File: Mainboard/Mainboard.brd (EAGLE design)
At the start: 90 x 150 mm, 9 parts, among them J1 USB3076-XX-X_REVC, J2 640455-5, J3 640455-2, J4 640455-4, J5 640455-4, J6 SJ-3523-SMT-TR, J7 640455-2, J8 929850-01-06-RB

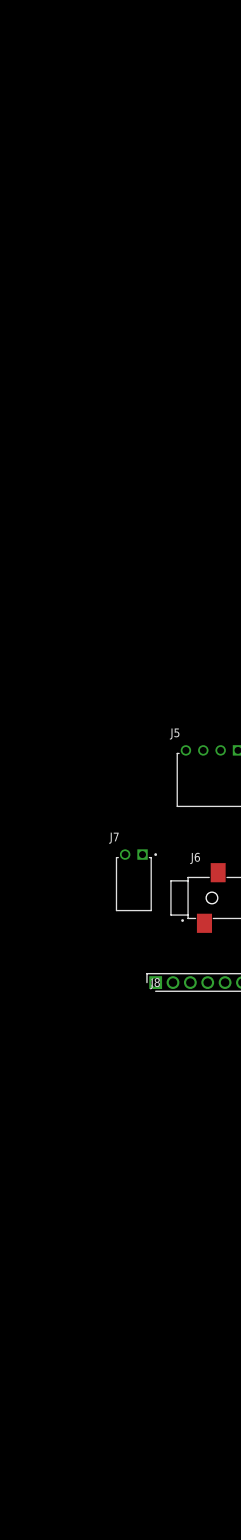
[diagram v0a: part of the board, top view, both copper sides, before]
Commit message: Mainboard updated
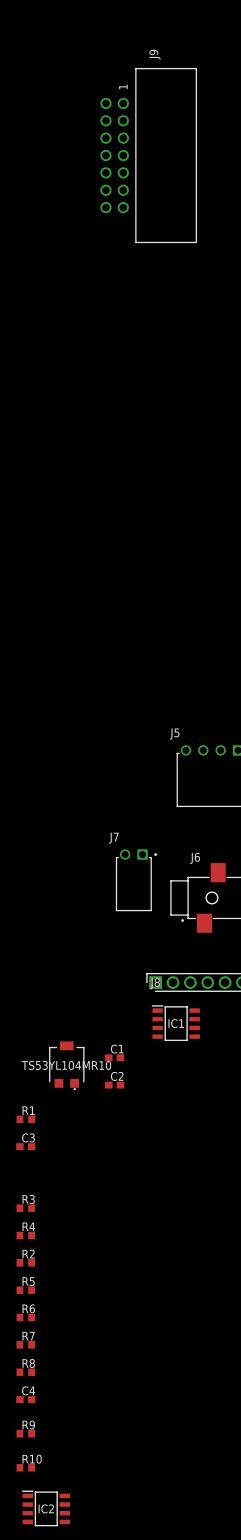
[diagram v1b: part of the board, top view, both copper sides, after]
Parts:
- added C1, C2: 100n, rcl:C0603
- added C3, C4: 1u, rcl:C0603
- added IC1: TL072CD, SamacSys_Parts:SOIC127P600X175-8N
- added IC2: LM386M-1_NOPB, SamacSys_Parts:SOIC127P600X175-8N
- added J9: 61201421721, 61201421721:61201421721
- added R1, R9: 10k, rcl:R0603
- added R10, R2, R3: 0, rcl:R0603
- added R4: NP_0, rcl:R0603
- added R5: 4k7, rcl:R0603
- added R6: 15k, rcl:R0603
- added R7: 33k, rcl:R0603
- added R8: 100, rcl:R0603
- added TS53YL104MR10: 100k, SamacSys_Parts:TS53YL203MR10
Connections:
- net E5V_CN11 renamed N$1
- removed net GND_CN12: A1.CN12_20, A1.CN12_39, A1.CN12_54, A1.CN12_63, A1.CN12_71, A1.CN12_72, A1.CN12_9
- new net +3V3: J9.8
- new net 1_IN+: C3.2, IC1.3, R1.2, R5.1
- new net 1_IN-: IC1.2, R2.1
- new net 1_OUT: C3.1, IC1.1, R3.1
- new net 2_IN-: IC1.6, R6.2, R7.1
- new net 2_OUT: IC1.7, R7.2, R8.1
- new net ADC_POTI: J9.9
- new net BUTTON_BACK: J9.13
- new net BUTTON_ENTER: J9.14
- new net DAC_OUT1: R10.1
- new net DISP_BUSY: J9.1
- new net DISP_CLK: J9.5
- new net DISP_CS: J9.4
- new net DISP_DC: J9.3
- new net DISP_DIN: J9.6
- new net DISP_RST: J9.2
- new net JOYSTICK_SW: J9.10
- new net JOYSTICK_VRX: J9.11
- new net JOYSTICK_VRY: J9.12
- new net N$10: A1.CN12_22
- new net N$11: A1.CN12_31
- new net N$12: A1.CN12_29
- new net N$13: A1.CN11_38
- new net N$14: A1.CN11_35
- new net N$15: A1.CN12_2
- new net N$16: A1.CN12_1
- new net N$17: A1.CN11_1
- new net N$18: R10.2
- new net N$19: R2.2, R3.2, R4.1
- new net N$2: A1.CN11_28
- new net N$20: R5.2, TS53YL104MR10.1
- new net N$21: R6.1, TS53YL104MR10.2
- new net N$22: C4.1, R8.2
- new net N$3: A1.CN12_35
- new net N$4: A1.CN12_37
- new net N$5: A1.CN11_32
- new net N$6: A1.CN12_11
- new net N$7: A1.CN12_13
- new net N$8: A1.CN11_34
- new net N$9: A1.CN12_24
- net +5V: now also C2.2, IC1.8
- net -5V: now also C1.2, IC1.4
- net GND: now also A1.CN12_20, A1.CN12_39, A1.CN12_54, A1.CN12_63, A1.CN12_71, A1.CN12_72, A1.CN12_9, C1.1, C2.1, IC1.5, J9.7, R1.1, R4.2, R9.1, TS53YL104MR10.3
- net PREAMP_AUDIO_OUT: now also C4.2, R9.2

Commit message: Mainboard updated II
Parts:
- added C10, C7: 1m, rcl:E2,5-5
- added C11: 1u, rcl:C0603
- added C5, C6: 100u, rcl:E2,5-5
- added C8: 100n, rcl:C0603
- added C9: NP_10u, rcl:C0603
- added R11: NP_1k2, rcl:R0603
- added R12, R13: 0, rcl:R0603
- added R14: 10k, rcl:R0603
- added TS53YL104MR1: 10k, SamacSys_Parts:TS53YL203MR10
- J3: value 640455-2 -> 640455-3; device 640455-2:TE_640455-2 -> 640455-3:TE_640455-3
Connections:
- net N$3 renamed USART2_TX
- net N$4 renamed USART2_RX
- removed net N$10: A1.CN12_22
- removed net N$11: A1.CN12_31
- removed net N$12: A1.CN12_29
- removed net N$13: A1.CN11_38
- removed net N$14: A1.CN11_35
- removed net N$15: A1.CN12_2
- removed net N$16: A1.CN12_1
- removed net N$17: A1.CN11_1
- removed net N$2: A1.CN11_28
- removed net N$5: A1.CN11_32
- removed net N$6: A1.CN12_11
- removed net N$7: A1.CN12_13
- removed net N$8: A1.CN11_34
- removed net N$9: A1.CN12_24
- new net ADC_EMG_AC: A1.CN11_11
- new net ADC_EMG_DC: A1.CN11_9
- new net ADC_KEYS: A1.CN11_35, C11.1, R14.2
- new net DAC_OUT2: A1.CN12_11, R13.1
- new net GYRO_I2C_SCL: A1.CN11_51
- new net GYRO_I2C_SDA: A1.CN11_53
- new net N$23: IC2.1, R11.1
- new net N$24: IC2.3, TS53YL104MR1.2
- new net N$25: C9.1, R11.2
- new net N$26: C9.2, IC2.8
- new net N$27: R12.2, TS53YL104MR1.1
- new net N$28: C5.+, IC2.7
- new net N$29: C7.+, C8.1, IC2.5
- new net USART3_RX: A1.CN11_69
- new net USART3_TX: A1.CN12_10
- net +5V: now also A1.CN11_6, C10.+, C6.+, IC2.6
- net 1_OUT: now also R12.1
- net ADC_POTI: now also A1.CN11_38
- net BUTTON_BACK: now also A1.CN12_1
- net BUTTON_ENTER: now also A1.CN12_40
- net DAC_OUT1: now also A1.CN11_32
- net DISP_BUSY: now also A1.CN12_24
- net DISP_CLK: now also A1.CN12_31
- net DISP_CS: now also A1.CN12_2
- net DISP_DC: now also A1.CN11_28
- net DISP_DIN: now also A1.CN12_29
- net DISP_RST: now also A1.CN12_59
- net GND: now also C10.-, C11.2, C5.-, C6.-, C8.2, IC2.2, IC2.4, TS53YL104MR1.3
- net JOYSTICK_SW: now also A1.CN11_59
- net JOYSTICK_VRX: now also A1.CN12_13
- net JOYSTICK_VRY: now also A1.CN11_34
- net N$1: now also J3.3, R14.1; no longer A1.CN11_6
- net N$18: now also R13.2
- net POWERAMP_AUDIO_OUT: now also C7.-
- net SD_CLK: now also A1.CN11_1
- net SD_CS: now also A1.CN12_42
- net SD_DI: now also A1.CN12_22
- net SD_DO: now also A1.CN11_2

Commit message: # Mainboard updated
# Keyboard V2:

	# Bug fixed (lowest Pad not GND)
	# 1 more key (upper C)
	# PEACE sign corrected

# General cleanup
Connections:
- net JOYSTICK_VRX renamed ADC_JOYSTICK_VRX
- net JOYSTICK_VRY renamed ADC_JOYSTICK_VRY
- removed net +3V3_CN11: A1.CN11_16
- removed net AC_OUT: J2.2
- removed net AGND_CN10: A1.CN10_3
- removed net DC_OUT: J2.3
- removed net GND_CN10: A1.CN10_17, A1.CN10_22, A1.CN10_27, A1.CN10_5
- removed net GND_CN7: A1.CN7_8
- removed net GND_CN8: A1.CN8_11, A1.CN8_13
- removed net GND_CN9: A1.CN9_12, A1.CN9_23
- removed net GYRO_SCL: J5.2
- removed net GYRO_SDA: J5.1
- removed net UC_AUDIO_OUT: J4.4
- net +3V3: now also A1.CN11_16, J3.2
- net 3V3: no longer J3.2
- net ADC_EMG_AC: now also J2.2
- net ADC_EMG_DC: now also J2.3
- net DAC_OUT1: now also J4.4
- net GND: now also A1.CN10_17, A1.CN10_22, A1.CN10_27, A1.CN10_3, A1.CN10_5, A1.CN7_8, A1.CN8_11, A1.CN8_13, A1.CN9_12, A1.CN9_23
- net GYRO_I2C_SCL: now also J5.2
- net GYRO_I2C_SDA: now also J5.1

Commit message: Mainboard updated IV
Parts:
- added C12: 4u7, rcl:C0603
- added C13, C14: 22u, rcl:C0603
- added R15, R16: 100k, rcl:R0603
- added R17, R18, R19: 1Meg, rcl:R0603
- added U1: MAX889RESA, MAX889RESA:SOIC127P600X175-8N
- moved C11 459.4 mm to (214.0, 118.0), turned to 90 degrees
- moved R14 452.4 mm to (209.0, 118.0), turned to 90 degrees
- moved R13 445.4 mm to (204.0, 118.0), turned to 90 degrees
- moved C10 436.8 mm to (198.0, 119.0), turned to 90 degrees
- moved R12 428.6 mm to (192.0, 118.0), turned to 90 degrees
- moved C9 421.6 mm to (187.0, 118.0), turned to 90 degrees
- moved R11 414.7 mm to (182.0, 118.0), turned to 90 degrees
- moved C8 407.7 mm to (177.0, 118.0), turned to 90 degrees
- moved C7 398.1 mm to (172.0, 131.0), turned to 90 degrees
- moved TS53YL104MR1 395.4 mm to (169.0, 123.0), turned to 90 degrees
- moved C5 381.3 mm to (160.0, 131.0), turned to 90 degrees
- moved IC2 372.0 mm to (154.0, 136.0), turned to 90 degrees
- moved R10 364.1 mm to (148.0, 133.0), turned to 90 degrees
- moved R9 357.1 mm to (143.0, 133.0), turned to 90 degrees
- moved C4 350.0 mm to (138.0, 133.0), turned to 90 degrees
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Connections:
- new net N$3: R15.1, R16.2, U1.7
- new net N$5: C12.2, U1.2
- new net N$6: C12.1, U1.4
- net +5V: now also C14.2, R16.1, U1.1, U1.6
- net -5V: now also C13.2, R15.2, U1.5
- net ADC_JOYSTICK_VRX: now also R19.2
- net ADC_JOYSTICK_VRY: now also R18.2
- net ADC_POTI: now also R17.2
- net GND: now also C13.1, C14.1, R17.1, R18.1, R19.1, U1.3, U1.8
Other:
- board size 90 x 150 mm -> 150 x 100 mm
- board text added: "EMG"
- board text added: "EQ"
- board text added: "FEET"
- board text added: "GYRO"
- board text added: "HEAD"
- board text added: "KEYS"
- board text added: "LEFT ARM"
- board text added: "RIGHT ARM"
- board text added: "SPEAKER"
- board text added: "USER INTERFACE"

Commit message: # Mainboard updated V
# Keys finalizing production
# EQ finalizing production
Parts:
- J1: value USB3076-XX-X_REVC -> USB3076
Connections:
- removed net 3V3: J8.1
- net +3V3: now also J8.1
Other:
- board text added: "+ 5 V"
- board text added: "+3V3"
- board text added: "- 5 V"
- board text added: "3 V 3"
- board text added: "A C"
- board text added: "B E R L I N"
- board text added: "CLK"
- board text added: "CS"
- board text added: "D C"
- board text added: "DI"
- board text added: "DO"
- board text added: "DSP-LAB SS21"
- board text added: "G N D"
- board text added: "GND"
- board text added: "HEAD- PHONES"
- board text added: "O U T"
- board text added: "P"
- board text added: "P E N"
- board text added: "Q"
- board text added: "R"
- board text added: "R I N G"
- board text added: "S"
- board text added: "S C L"
- board text added: "S D A"
- board text added: "S L E"
- board text added: "T"
- board text added: "T I P"
- board text added: "The Body-Synth"
- board text added: "U"
- board text added: "V C C"

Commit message: Mainboard updated VI (ready2route)
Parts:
- moved C14 250.1 mm to (6.00, 17.0), turned to 270 degrees
- moved R16 238.7 mm to (12.8, 18.4), turned to 0 degrees
- moved C12 233.0 mm to (6.00, 13.5)
- moved C13 230.2 mm to (20.0, 11.5)
- moved R15 224.2 mm to (20.0, 15.0), turned to 270 degrees
- moved U1 221.4 mm to (12.8, 14.3), turned to 0 degrees
- moved R13 204.8 mm to (30.0, 10.0), turned to 0 degrees
- moved C10 203.3 mm to (9.60, 42.7), turned to 270 degrees
- moved R10 169.0 mm to (30.0, 12.0), turned to 0 degrees
- moved C11 167.5 mm to (102.3, -6.80), turned to 180 degrees
- moved R12 163.4 mm to (63.0, 17.7), turned to 0 degrees
- moved R14 162.0 mm to (105.7, -6.80), turned to 180 degrees
- moved R9 157.6 mm to (47.0, 8.00), turned to 270 degrees
- moved C4 156.9 mm to (44.2, 7.20), turned to 0 degrees
- moved R8 155.5 mm to (41.5, 8.00), turned to 270 degrees
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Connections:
- removed net N$18: R10.2, R13.2
- new net N$2: C3.2, R1.2, R5.1
- net 1_IN+: now also R10.2, R13.2; no longer C3.2, R1.2, R5.1
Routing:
- net GND: track 0.00 -> 65.6 mm
- net +5V: track 0.00 -> 27.5 mm, vias 0 -> 2
- net 2_OUT: track 0.00 -> 16.1 mm
- net N$28: track 0.00 -> 12.2 mm
- net N$3: track 0.00 -> 12.0 mm
- net 2_IN-: track 0.00 -> 12.0 mm
- net -5V: track 0.00 -> 11.6 mm
- net 1_IN+: track 0.00 -> 11.4 mm
- net N$29: track 0.00 -> 9.61 mm
- net N$24: track 0.00 -> 9.50 mm
- net 1_OUT: track 0.00 -> 7.77 mm
- net N$21: track 0.00 -> 5.60 mm
- net N$20: track 0.00 -> 5.35 mm
- net N$5: track 0.00 -> 4.91 mm
- net N$6: track 0.00 -> 4.58 mm
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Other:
- board size 150 x 100 mm -> 150 x 115 mm
- board text added: "!SHDN!"
- board text added: "-5V"
- board text added: "1IN+"
- board text added: "1IN-"
- board text added: "1OUT"
- board text added: "2IN+"
- board text added: "2IN-"
- board text added: "2OUT"
- board text added: "AGND"
- board text added: "BYPASS"
- board text added: "CAP+"
- board text added: "CAP-"
- board text added: "DAC_OUT1"
- board text added: "DAC_OUT2"
- board text added: "FB"
- board text added: "GAIN"
- board text added: "IN"
- board text added: "IN+"
- board text added: "IN-"
- board text added: "OUT"
- board text added: "PREAMP"
- board text added: "PWR AMP"
- board text added: "VCC"
- board text added: "VCC+"
- board text added: "VCC-"

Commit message: Mainboard updated VII
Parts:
- added C15, C16, C17, C18, C19, C20, C21, C22, C23, C24: 1u, rcl:C0603
- moved J1 147.8 mm to (148.6, 57.3), turned to 90 degrees
- moved C10 132.6 mm to (141.4, 57.3), turned to 90 degrees
- moved R16 126.8 mm to (137.8, 39.4)
- moved U1 126.8 mm to (137.8, 35.3)
- moved C12 126.8 mm to (131.0, 34.5)
- moved C13 126.8 mm to (145.0, 32.5)
- moved C14 126.8 mm to (131.0, 38.0)
- moved R15 126.8 mm to (145.0, 36.0)
- moved R19 117.4 mm to (53.8, 116.6), turned to 0 degrees
- moved R17 26.6 mm to (107.4, 43.0), turned to 90 degrees
- moved R18 26.6 mm to (109.9, 43.0), turned to 90 degrees
- moved J5 15.1 mm to (30.6, 8.17)
- moved J4 15.0 mm to (86.0, 8.17)
- moved R12 15.0 mm to (63.0, 32.7)
- moved C6 15.0 mm to (84.0, 28.1)
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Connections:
- removed net VCC: J5.4
- net +3V3: now also C19.2, C20.2, C21.2, C22.2, J5.4
- net +5V: now also C15.2, C16.2, C17.2, C18.2
- net -5V: now also C23.2, C24.2
- net GND: now also C15.1, C16.1, C17.1, C18.1, C19.1, C20.1, C21.1, C22.1, C23.1, C24.1
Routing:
- net GND: track 65.6 -> 687.8 mm, vias 0 -> 2
- net +5V: track 27.5 -> 378.8 mm
- net +3V3: track 0.00 -> 275.2 mm, vias 0 -> 3
- net BUTTON_BACK: track 0.00 -> 245.3 mm, vias 0 -> 1
- net ADC_JOYSTICK_VRX: track 0.00 -> 226.9 mm, vias 0 -> 2
- net DISP_CS: track 0.00 -> 209.6 mm, vias 0 -> 1
- net DISP_BUSY: track 0.00 -> 187.4 mm
- net DISP_CLK: track 0.00 -> 173.4 mm
- net DISP_DIN: track 0.00 -> 170.8 mm
- net -5V: track 11.6 -> 178.8 mm
- net DISP_RST: track 0.00 -> 161.7 mm
- net BUTTON_ENTER: track 0.00 -> 159.1 mm
- net DISP_DC: track 0.00 -> 131.7 mm
- net ADC_JOYSTICK_VRY: track 0.00 -> 118.8 mm, vias 0 -> 2
- net ADC_KEYS: track 0.00 -> 116.5 mm, vias 0 -> 1
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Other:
- board size 150 x 115 mm -> 150 x 120 mm
- board text removed: "V C C"

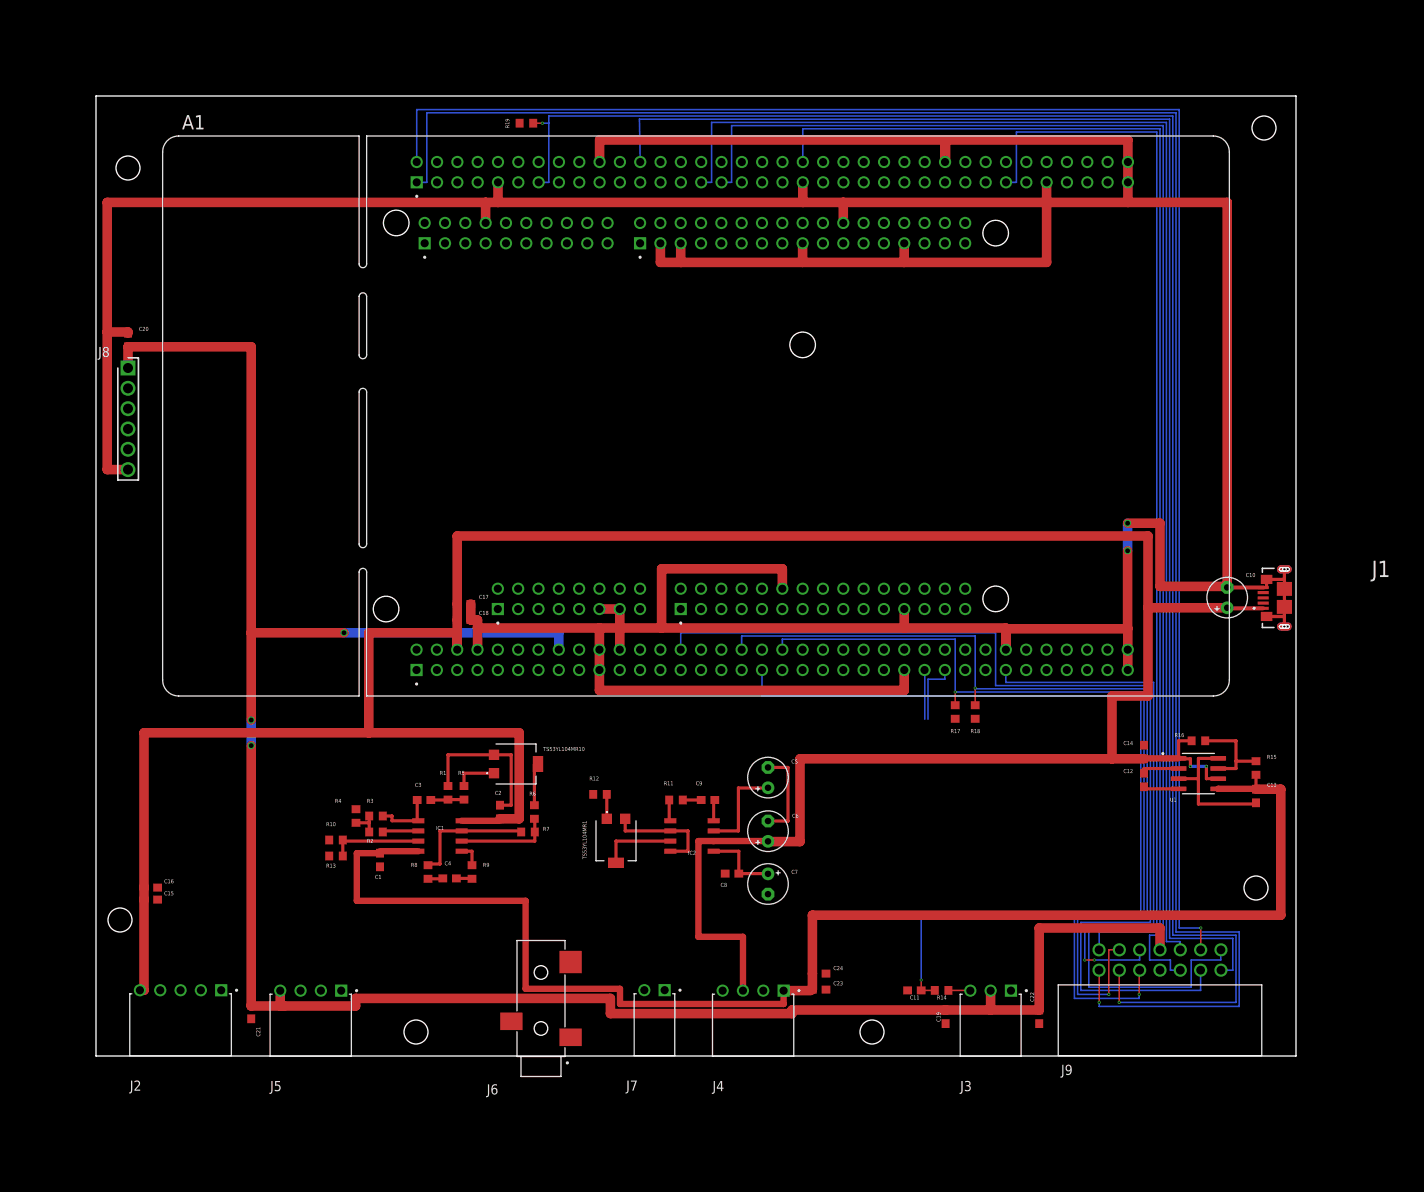
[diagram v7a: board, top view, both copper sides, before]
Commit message: Mainboard updated VIII: routed completely, only need to check SD Card size
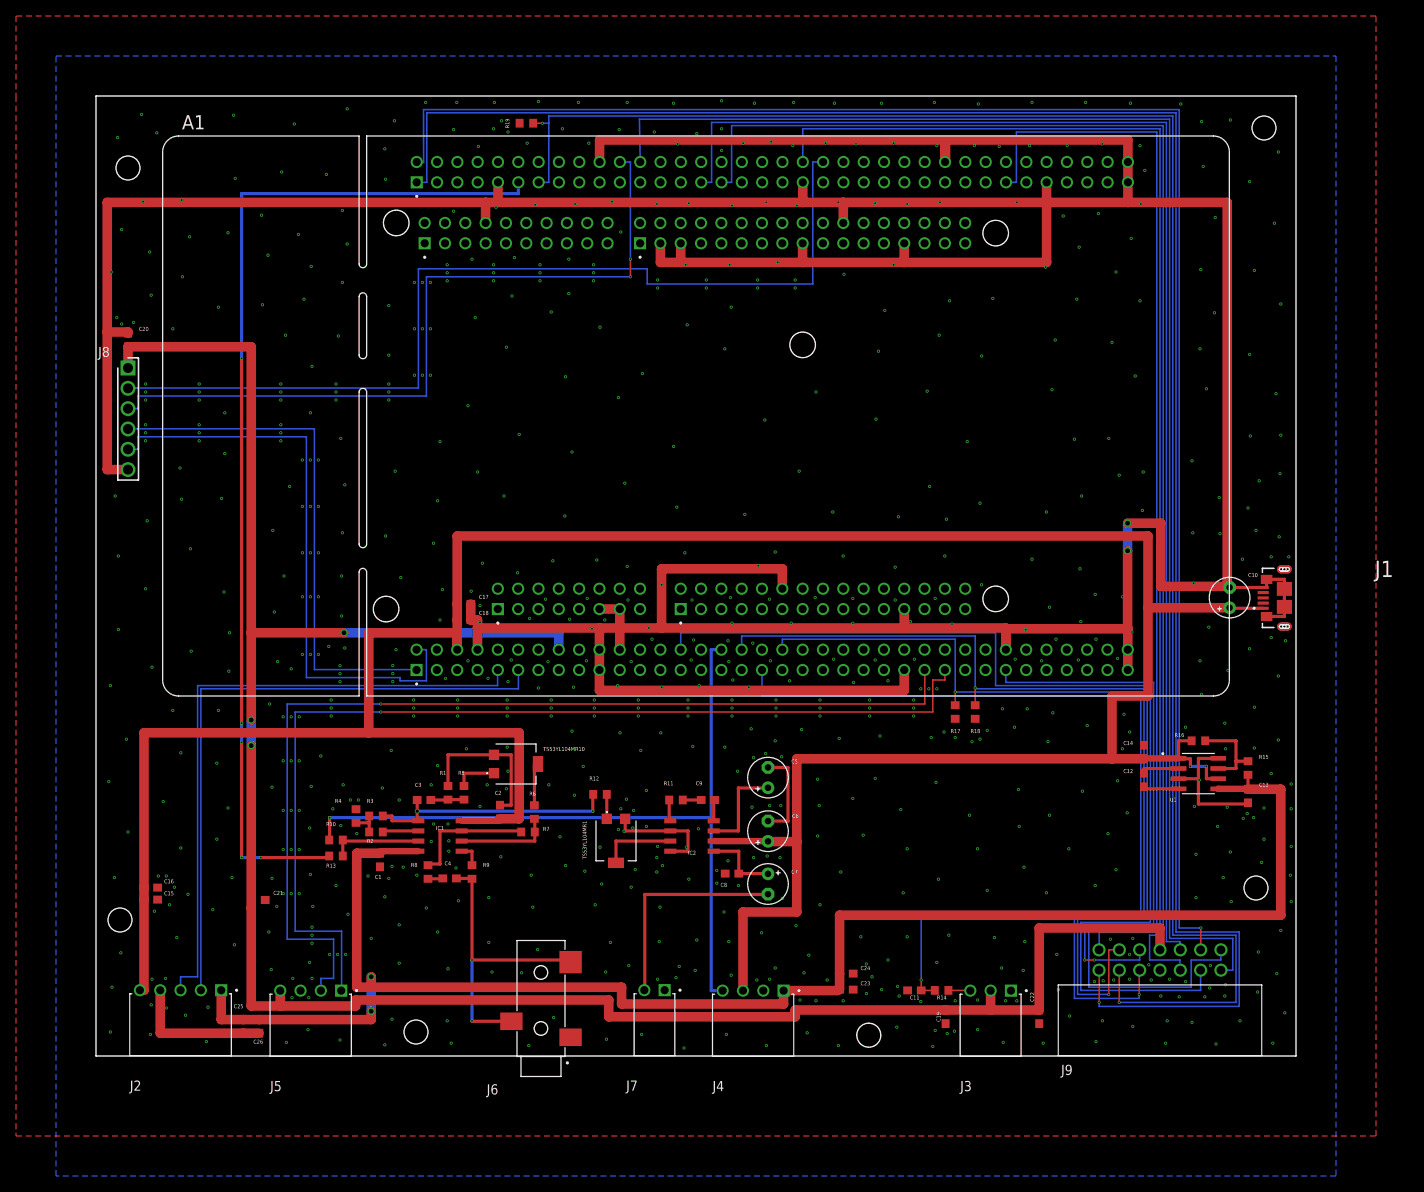
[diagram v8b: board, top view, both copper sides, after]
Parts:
- added C25, C26: 1u, rcl:C0603
- moved C21 14.0 mm to (20.3, 19.5), turned to 180 degrees
- moved C23 3.40 mm to (93.8, 8.30)
- moved C24 3.40 mm to (93.8, 10.3)
- moved C13 1.00 mm to (144.0, 32.5)
- moved R15 1.00 mm to (144.0, 36.0)
- moved C10 0.30 mm to (141.7, 57.3)
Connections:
- net -5V: now also C25.2, C26.2
- net GND: now also C25.1, C26.1
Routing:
- net DAC_OUT2: track 0.00 -> 130.2 mm, vias 0 -> 5
- net GYRO_I2C_SCL: track 6.18 -> 127.2 mm, vias 0 -> 1
- net SD_CS: track 0.00 -> 119.0 mm
- net GYRO_I2C_SDA: track 8.26 -> 127.1 mm, vias 0 -> 1
- net DAC_OUT1: track 0.00 -> 95.9 mm, vias 0 -> 1
- net SD_DI: track 0.00 -> 94.9 mm, vias 0 -> 2
- net ADC_EMG_AC: track 0.00 -> 79.8 mm
- net ADC_EMG_DC: track 0.00 -> 79.7 mm
- net SD_DO: track 0.00 -> 74.5 mm
- net SD_CLK: track 0.00 -> 66.2 mm
- net PREAMP_AUDIO_OUT: track 2.00 -> 37.3 mm, vias 0 -> 2
- net -5V: track 178.8 -> 209.8 mm, vias 0 -> 2
- net POWERAMP_AUDIO_OUT: track 0.00 -> 27.5 mm
- net 1_OUT: track 7.77 -> 32.0 mm, vias 0 -> 2
- net GND: track 687.8 -> 701.1 mm, vias 2 -> 784
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- added copper zone on layer 1, net GND
- added copper zone on layer 16, net GND
